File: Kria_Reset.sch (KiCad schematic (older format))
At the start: 28 parts, among them IC18 74AVC4T245RSVR-NT, J15 3220-10-0100-00, Q19 DMN26D0UFB4-7, Q20 DMN26D0UFB4-7, Q21 DMN26D0UFB4-7, U23 SN74AXC1T45DCKR, U4 PIC18LF47K42-I-MV

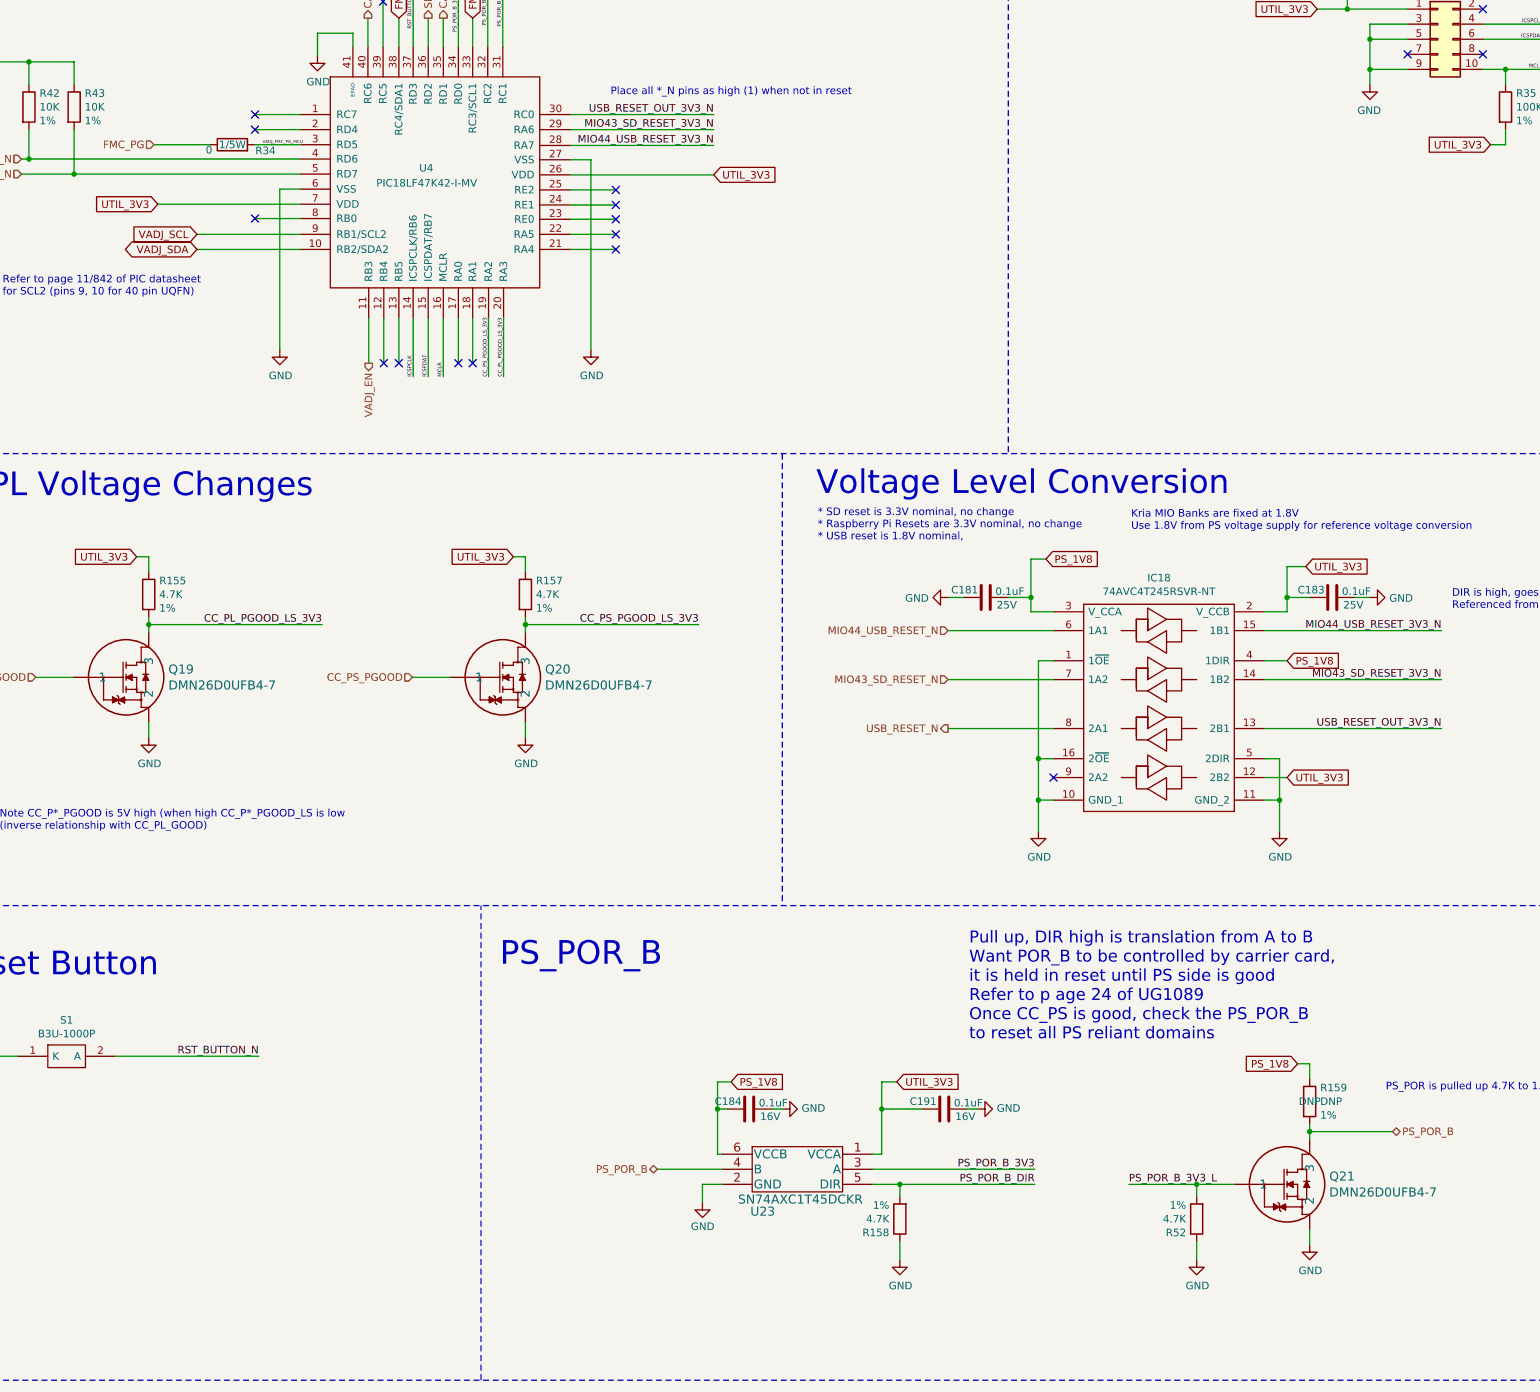
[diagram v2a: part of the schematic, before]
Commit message: Update to Kicad 7
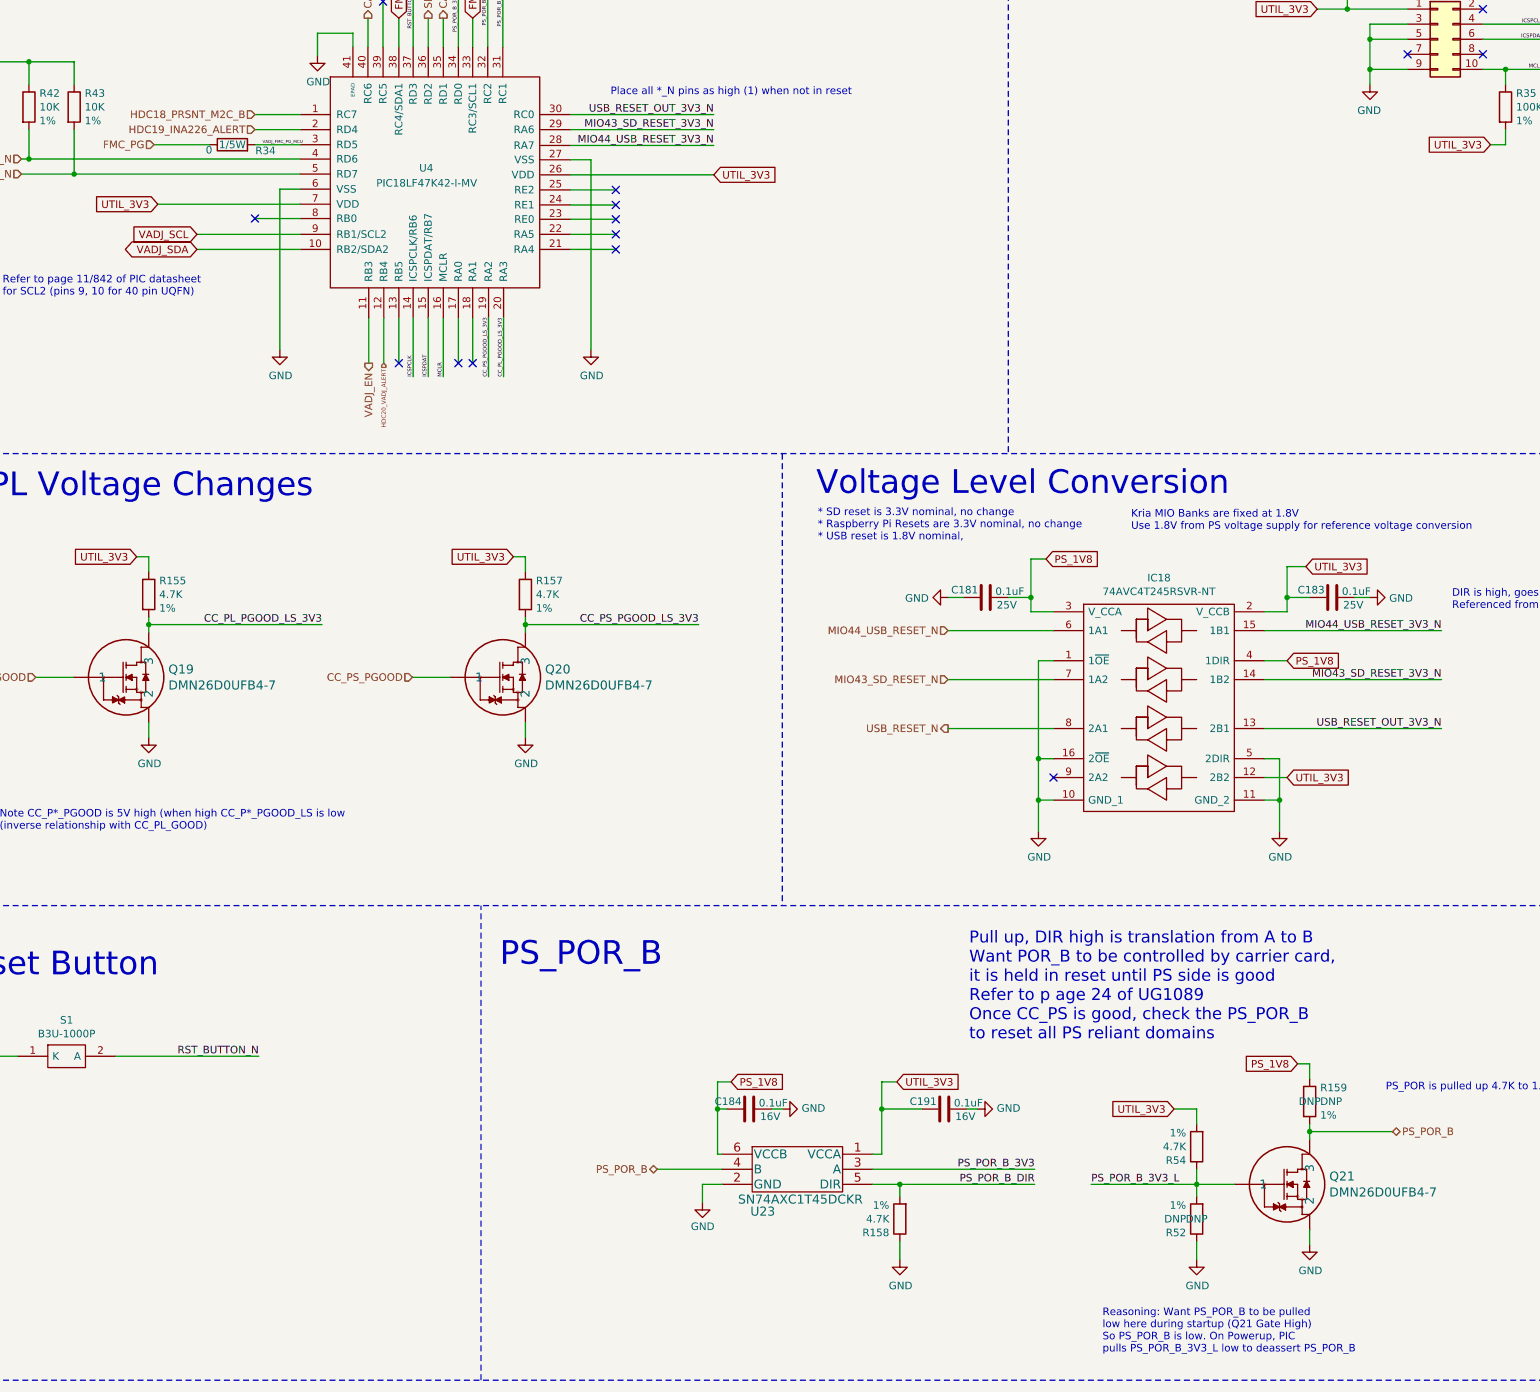
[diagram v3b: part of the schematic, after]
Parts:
- added R54: 4.7K, Resistor_SMD:R_0402_1005Metric, symbol Device:R
- R52: value 4.7K -> DNP; DNP (none) -> DNP
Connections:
- net PS_POR_B_3V3_L: now also R54.1
- net UTIL_3V3: now also R54.2
- net HDC18_PRSNT_M2C_B: now reaches U4.1 (RC7)
- net HDC20_VADJ_ALERT: now reaches U4.12 (RB4)
- net HDC19_INA226_ALERT: now reaches U4.2 (RD4)
- no-connect marks 17 -> 14
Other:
- note added: "Reasoning: Want PS_POR_B to be pulled \nlow here during startup (Q21 Gate High)\nSo PS_POR_B is low. On Powerup, PIC \npulls PS_POR_B_3V3_L low to deassert PS_POR_B"
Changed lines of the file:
@@
 Wire Wire Line
 	3300 2850 3000 2850
-NoConn ~ 3000 2850
 Wire Wire Line
 	3300 2750 3000 2750
-NoConn ~ 3000 2750
 Wire Wire Line
 	5095 3250 5395 3250
@@
 Wire Wire Line
 	3855 4100 3855 4400
-NoConn ~ 3855 4400
 Wire Wire Line
 	3955 4100 3955 4400
@@
 Wire Wire Line
 	10000 9450 10000 9500
-Wire Wire Line
-	8800 9850 9250 9850
-Text Label 8800 9850 0    50   ~ 0
+Text Label 8550 9850 0    50   ~ 0
 PS_POR_B_3V3_L
 $Comp
@@
 AR Path="/61AA736C/6348FECF" Ref="R52"  Part="1"
 F 0 "R52" H 9320 10171 50  0000 L CNN
-F 1 "4.7K" H 9320 10080 50  0000 L CNN
+F 1 "DNP" H 9320 10080 50  0000 L CNN
 F 2 "Resistor_SMD:R_0402_1005Metric" V 9180 10080 50  0001 C CNN
 F 3 "~" H 9250 10080 50  0001 C CNN
 F 4 "1%" H 9320 9989 50  0000 L CNN "Tolerance"
 F 5 "CRCW04024K70FKED" H 9250 10080 50  0001 C CNN "PartNumber"
+F 6 "DNP" H 9250 10080 50  0000 C CNN "DNP"
 	1    9250 10080
 	-1   0    0    1
@@
 Text Notes 10505 9235 0    50   ~ 0
 PS_POR is pulled up 4.7K to 1.8V on SOM
+Wire Wire Line
+	8550 9850 9250 9850
+$Comp
+L Device:R R?
+U 1 1 63C13053
+P 9250 9600
+AR Path="/5F71E87D/63C13053" Ref="R?"  Part="1"
+AR Path="/5F71E4A6/63C13053" Ref="R?"  Part="1"
+AR Path="/61AA736C/63C13053" Ref="R54"  Part="1"
+F 0 "R54" H 9320 9691 50  0000 L CNN
+F 1 "4.7K" H 9320 9600 50  0000 L CNN
+F 2 "Resistor_SMD:R_0402_1005Metric" V 9180 9600 50  0001 C CNN
+F 3 "~" H 9250 9600 50  0001 C CNN
+F 4 "1%" H 9320 9509 50  0000 L CNN "Tolerance"
+F 5 "CRCW04024K70FKED" H 9250 9600 50  0001 C CNN "PartNumber"
+	1    9250 9600
+	-1   0    0    1
+$EndComp
+Wire Wire Line
+	9250 9850 9250 9750
+Text GLabel 9100 9350 0    50   Input ~ 0
+UTIL_3V3
+Wire Wire Line
+	9100 9350 9250 9350
+Wire Wire Line
+	9250 9350 9250 9450
+Text Notes 8625 10975 0    50   ~ 0
+Reasoning: Want PS_POR_B to be pulled \nlow here during startup (Q21 Gate High)\nSo PS_POR_B is low. On Powerup, PIC \npulls PS_POR_B_3V3_L low to deassert PS_POR_B
+Text HLabel 3855 4400 3    28   Input ~ 0
+HDC20_VADJ_ALERT
+Text HLabel 3000 2850 0    50   Input ~ 0
+HDC19_INA226_ALERT
+Text HLabel 3000 2750 0    50   Input ~ 0
+HDC18_PRSNT_M2C_B
 $EndSCHEMATC
